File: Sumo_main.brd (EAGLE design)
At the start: 45 x 50 mm, 32 parts, among them U1 ATMEGA8U2AU, U2 SN65HVD3082ED, X1 MINI-USB-SCHIELD-32005-201, X2 RS485, X4 IR Sensor 1, X5 IR Sensor 2, X6 IR Sensor 3, Y1 16MHz

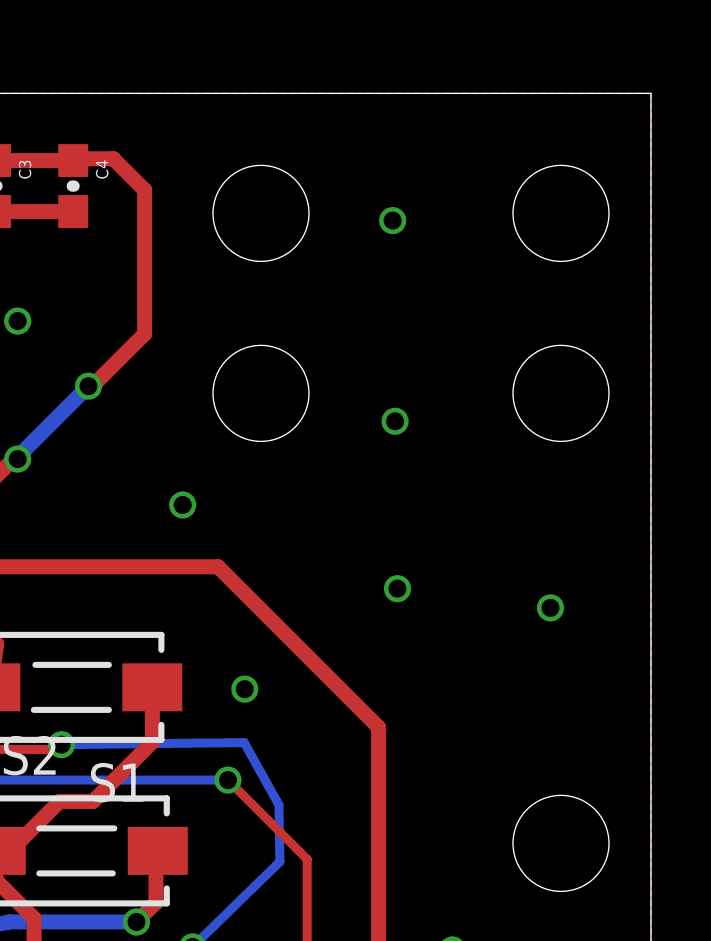
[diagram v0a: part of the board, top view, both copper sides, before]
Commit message: Added PNGs of schematic and board, added text to schematic and board and shortened some components' names.
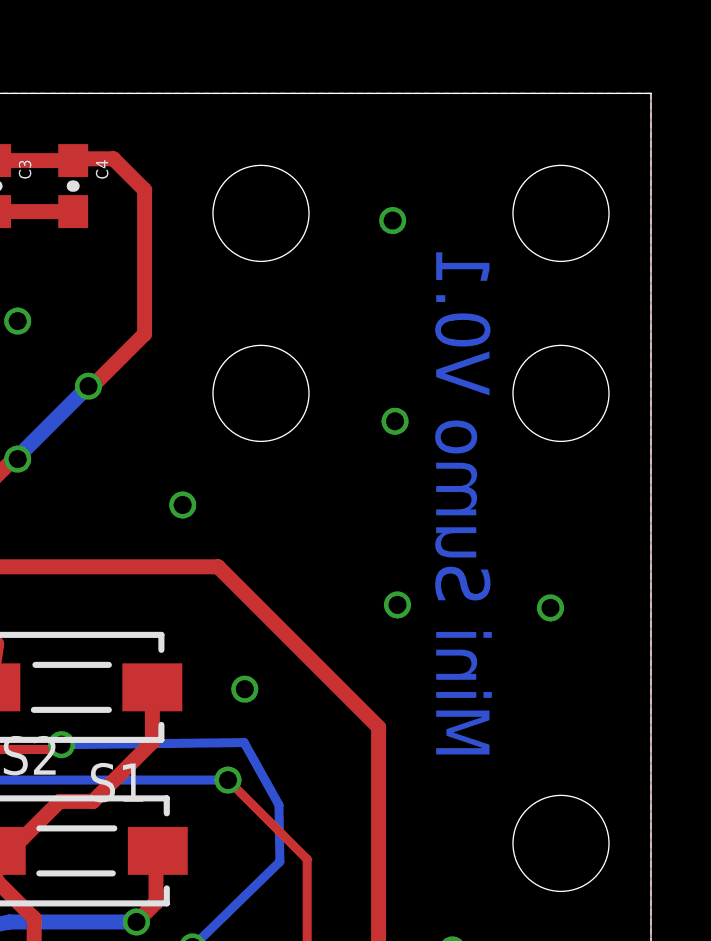
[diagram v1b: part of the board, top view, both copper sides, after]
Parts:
- U2: value SN65HVD3082ED -> SN65HVD3082
- X1: value MINI-USB-SCHIELD-32005-201 -> MINI USB
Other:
- board text added: "Mini Sumo V0.1"
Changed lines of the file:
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@@
 <hole x="32" y="46" drill="3.2"/>
 <hole x="32" y="40" drill="3.2"/>
+<text x="37.84" y="27.75" size="1.778" layer="16" rot="MR90">Mini Sumo V0.1</text>
 </plain>
 <attributes>
@@
 <element name="C3" library="SparkFun-Capacitors" package="0603-CAP" value="100nF" x="23.17" y="46.91" rot="R270"/>
 <element name="C4" library="SparkFun-Capacitors" package="0603-CAP" value="100nF" x="25.74" y="46.91" rot="R270"/>
-<element name="X1" library="con-cypressindustries" package="32005-201" value="MINI-USB-SCHIELD-32005-201" x="5.35" y="43.03">
+<element name="X1" library="con-cypressindustries" package="32005-201" value="MINI USB" x="5.35" y="43.03">
 <attribute name="OC_NEWARK" value="unknown" x="49.8" y="35.41" size="1.778" layer="27" display="off"/>
 <attribute name="MPN" value="" x="49.8" y="35.41" size="1.778" layer="27" display="off"/>
@@
 <attribute name="OC_FARNELL" value="unknown" x="-48.24" y="8.4" size="1.778" layer="27" rot="R270" display="off"/>
 </element>
-<element name="U2" library="SN65HVD3082ED" package="SOIC127P600X175-8N" value="SN65HVD3082ED" x="13.67" y="17.26" rot="R270">
+<element name="U2" library="SN65HVD3082ED" package="SOIC127P600X175-8N" value="SN65HVD3082" x="13.67" y="17.26" rot="R270">
 <attribute name="PACKAGE" value="SOIC-8" x="-10.46" y="-18.3" size="1.778" layer="27" rot="R270" display="off"/>
 <attribute name="OC_NEWARK" value="61H5396" x="-10.46" y="-18.3" size="1.778" layer="27" rot="R270" display="off"/>
@@
 </signal>
 <signal name="N$24">
-<via x="36.55" y="33.49" extent="1-16" drill="0.6"/>
+<via x="36.55" y="32.95" extent="1-16" drill="0.6"/>
 </signal>
 <signal name="N$25">
@@
 </signal>
 </signals>
+<errors>
+</errors>
 </board>
 </drawing>

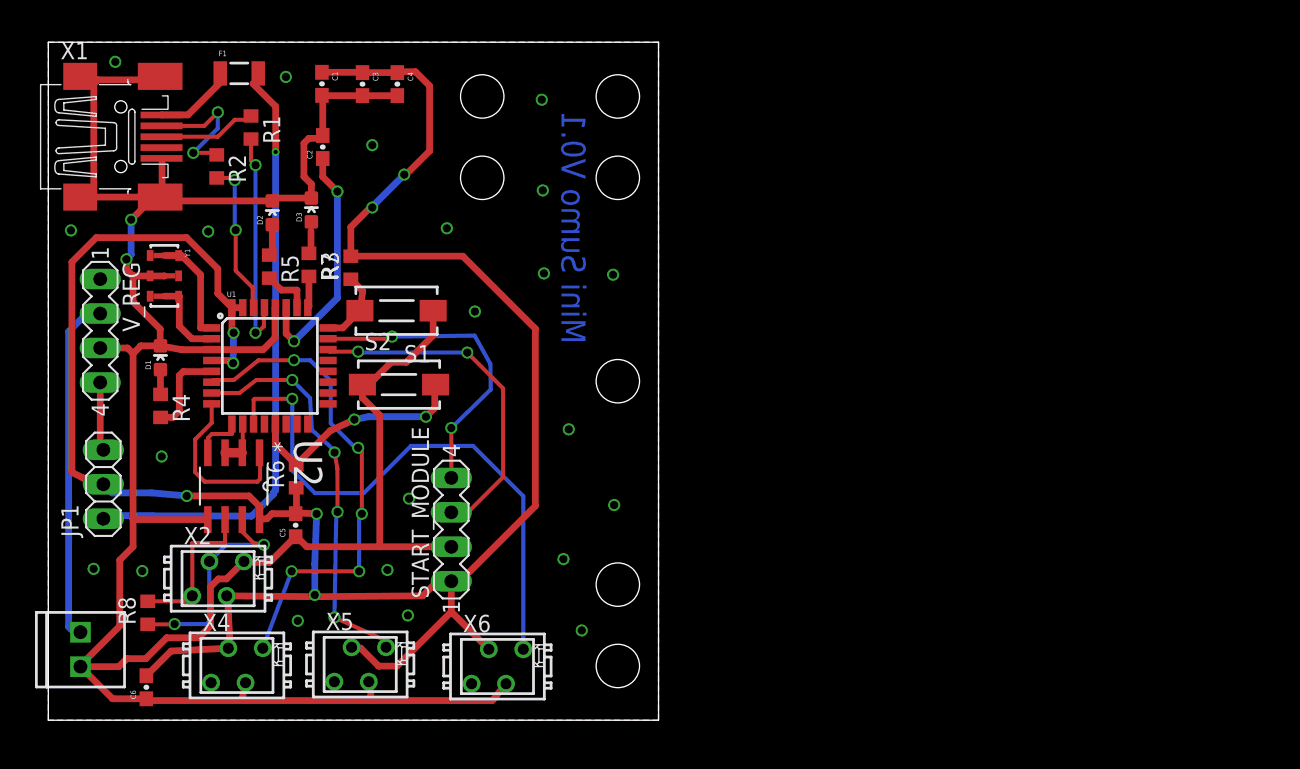
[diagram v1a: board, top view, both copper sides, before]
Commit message: Version 2 - added comparator for sensor signals, redesigned board to be more compact.
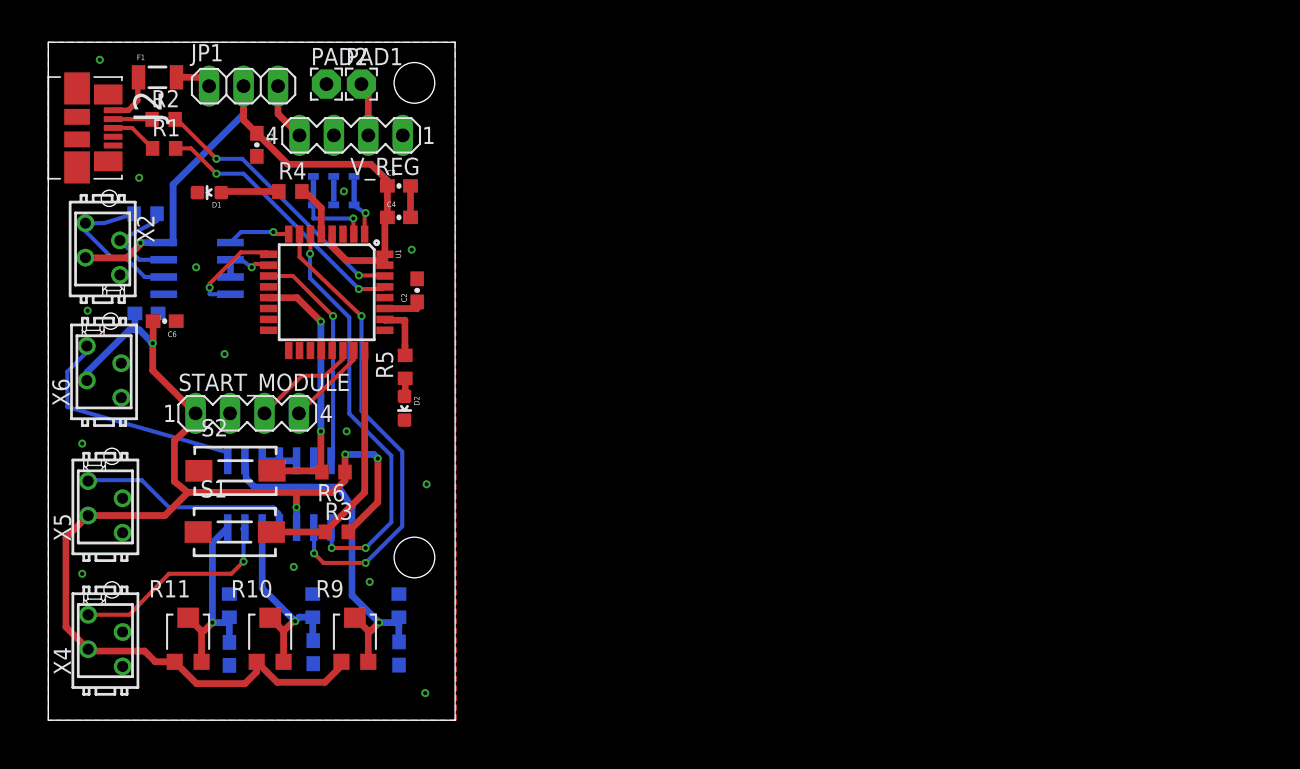
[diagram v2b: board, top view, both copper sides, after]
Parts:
- removed D3: (no value), SparkFun-LED:LED-0603
- removed J1: (no value), SparkFun-Connectors:1X02_2.54_SCREWTERM
- removed R7: 1K, resistor:R0603
- removed X1: MINI USB, con-cypressindustries:32005-201
- added C7, C8, C9: 1uF, SparkFun-Capacitors:0603-CAP
- added J2: (no value), Molex-47346-0001:MOLEX_47346-0001
- added PAD1, PAD2: (no value), wirepad:2,15/1,0
- added R10, R11, R9: 10KOHM, Panasonic-Trimmer_Potentiometers:POT_EVM3W
- added R12, R13, R14: 500R, resistor:R0603
- added U3: LM339D, comparator:SOIC127P600X175-14N
- moved X6 36.2 mm to (4.11, 25.7), turned to 90 degrees
- moved JP1 31.1 mm to (14.4, 46.8), turned to 0 degrees
- moved R8 29.4 mm to (7.17, 37.4), flipped to the bottom, turned to 0 degrees
- moved C6 27.0 mm to (8.58, 29.4), turned to 180 degrees
- moved X2 25.8 mm to (4.01, 34.8), turned to 270 degrees
- moved V_REG 23.4 mm to (22.3, 43.1), turned to 180 degrees
- moved X5 22.1 mm to (4.21, 15.7), turned to 90 degrees
- moved S1 20.2 mm to (13.8, 13.9), turned to 0 degrees
- moved R3 19.5 mm to (21.3, 13.9), turned to 0 degrees
- moved C5 19.1 mm to (7.24, 30.0), flipped to the bottom, turned to 0 degrees
- moved R4 18.5 mm to (17.9, 39.0), turned to 0 degrees
- moved D2 17.4 mm to (26.3, 23.0), turned to 180 degrees
- moved START_MODULE 17.3 mm to (14.7, 22.6), turned to 0 degrees
- moved U2 16.3 mm to (11.0, 33.3), flipped to the bottom, turned to 0 degrees
- moved Y1 14.0 mm to (21.1, 39.0), flipped to the bottom, turned to 0 degrees
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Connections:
- removed net LED3: R7.2, U1.25
- removed net N$8: D3.A, R7.1
- new net COMP_OUT1: U1.6, U3.1
- new net COMP_OUT2: U1.7, U3.2
- new net COMP_OUT3: U1.11, U3.14
- new net VREF1: C7.1, R11.2, R11.3, R14.2, U3.7
- new net VREF2: C9.1, R10.2, R10.3, R13.2, U3.5
- new net VREF3: C8.1, R12.2, R9.2, R9.3, U3.9
- net GND: now also C7.2, C8.2, C9.2, J2.5, PAD2.1, R12.1, R13.1, R14.1, U3.10, U3.11, U3.12; no longer D3.C, J1.P2, X1.5, X1.M1, X1.M2, X1.M3, X1.M4
- net N$1: now also J2.3; no longer X1.3
- net N$2: now also J2.2; no longer X1.2
- net N$23: now also PAD1.1; no longer J1.P1
- net N$3: now also J2.1; no longer X1.1
- net V01: now also U3.6; no longer U1.6
- net V02: now also U3.4; no longer U1.7
- net V03: now also U3.8; no longer U1.11
- net VCC: now also R10.1, R11.1, R9.1, U3.3
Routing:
- net GND: track 204.9 -> 4.86 mm, vias 2 -> 14
- net N$12: track 45.2 -> 2.68 mm, vias 1 -> 0
- net VCC: track 174.5 -> 137.9 mm, vias 7 -> 5
- net COMP_OUT2: track 0.00 -> 34.6 mm, vias 0 -> 3
- net COMP_OUT1: track 0.00 -> 30.5 mm, vias 0 -> 3
- net VREF3: track 0.00 -> 27.6 mm, vias 0 -> 1
- net V03: track 41.9 -> 18.0 mm, vias 1 -> 0
- net N$23: track 26.2 -> 4.00 mm
- net V01: track 36.2 -> 15.7 mm, vias 5 -> 1
- net START: track 25.5 -> 8.06 mm, vias 2 -> 0
- net COMP_OUT3: track 0.00 -> 16.7 mm, vias 0 -> 1
- net KILL: track 22.9 -> 6.34 mm, vias 2 -> 0
- net VREF2: track 0.00 -> 15.9 mm, vias 0 -> 1
- net VREF1: track 0.00 -> 15.5 mm, vias 0 -> 1
- net N$7: track 18.0 -> 2.87 mm, vias 2 -> 0
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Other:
- board size 45 x 50 mm -> 30 x 50 mm
- board text removed: "Mini Sumo V0.1"

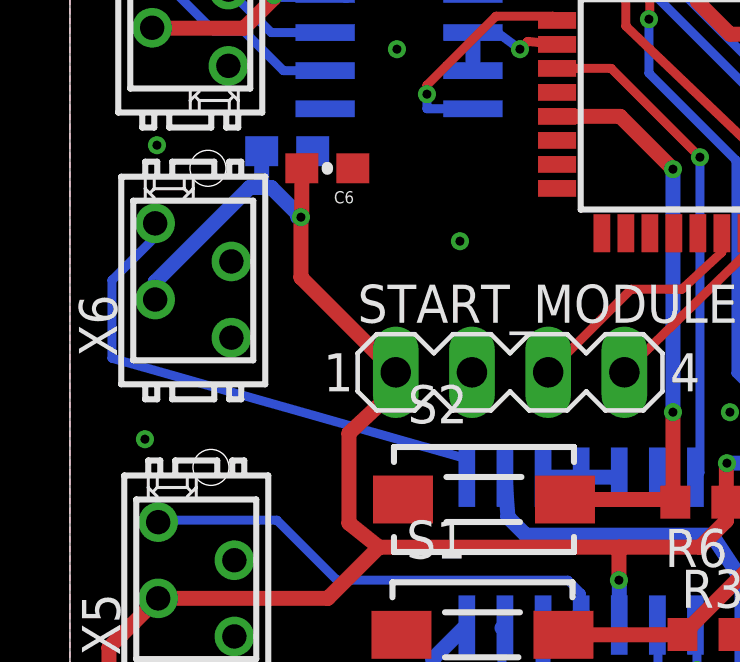
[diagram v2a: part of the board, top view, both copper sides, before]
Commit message: Re-routed X6 signal and VCC.
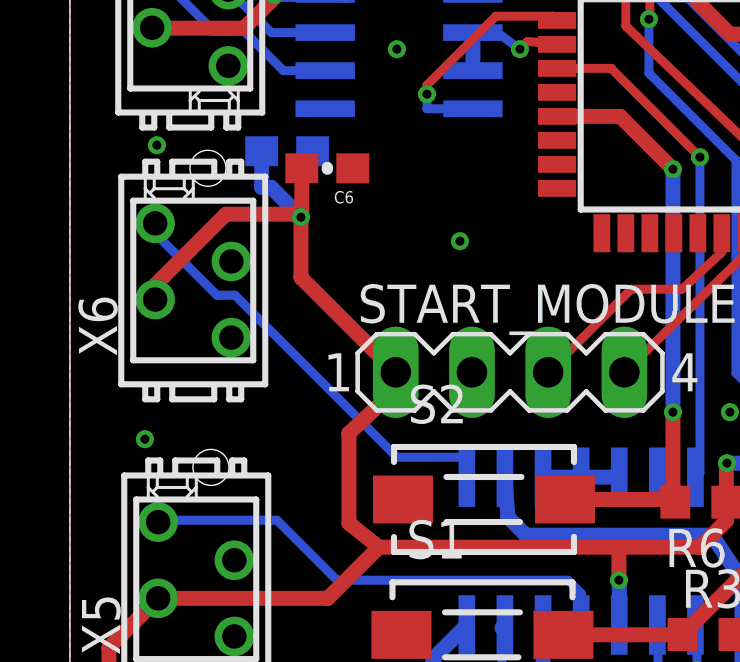
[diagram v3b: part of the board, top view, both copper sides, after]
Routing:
- net V03: track 18.0 -> 14.5 mm
- net VCC: track 137.9 -> 138.8 mm
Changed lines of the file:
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@@
 <wire x1="24.8226" y1="36.8926" x2="24.8226" y2="34.36" width="0.5" layer="1"/>
 <wire x1="24.8226" y1="34.36" x2="24.8226" y2="33.56" width="0.5" layer="1"/>
-<wire x1="5.99" y1="28.79" x2="2.84" y2="25.64" width="0.5" layer="16"/>
-<wire x1="2.84" y1="25.64" x2="2.84" y2="25.055" width="0.5" layer="16"/>
 <wire x1="7.59" y1="27.8" x2="7.7" y2="27.8" width="0.5" layer="16"/>
 <via x="7.7" y="27.8" extent="1-16" drill="0.3"/>
@@
 <wire x1="21.9" y1="19.6" x2="21.88" y2="19.58" width="0.5" layer="1"/>
 <wire x1="21.88" y1="19.58" x2="21.88" y2="18.3" width="0.5" layer="1"/>
-<wire x1="5.99" y1="28.79" x2="6.4" y2="28.79" width="0.5" layer="16"/>
 <wire x1="6.4" y1="28.79" x2="6.71" y2="28.79" width="0.5" layer="16"/>
 <wire x1="6.71" y1="28.79" x2="7.7" y2="27.8" width="0.5" layer="16"/>
@@
 <wire x1="9.3" y1="20.6" x2="10.86" y2="22.06" width="0.5" layer="1"/>
 <wire x1="10.86" y1="22.06" x2="10.86" y2="22.63" width="0.5" layer="1"/>
+<wire x1="2.84" y1="25.055" x2="2.84" y2="25.54" width="0.5" layer="1"/>
+<wire x1="2.84" y1="25.54" x2="5.2" y2="27.9" width="0.5" layer="1"/>
+<wire x1="5.2" y1="27.9" x2="7.6" y2="27.9" width="0.5" layer="1"/>
+<wire x1="7.6" y1="27.9" x2="7.7" y2="27.8" width="0.5" layer="1"/>
 <wire x1="6.39" y1="30" x2="5.8" y2="34.1" width="0" layer="19" extent="1-16"/>
 </signal>
@@
 <contactref element="X6" pad="1"/>
 <contactref element="U3" pad="8"/>
-<wire x1="2.84" y1="27.595" x2="2.84" y2="27.14" width="0.3" layer="16"/>
-<wire x1="2.84" y1="27.14" x2="1.4" y2="25.7" width="0.3" layer="16"/>
-<wire x1="1.4" y1="25.7" x2="1.4" y2="23.1" width="0.3" layer="16"/>
-<wire x1="1.4" y1="23.1" x2="13.2662" y2="19.7338" width="0.3" layer="16"/>
-<wire x1="13.2662" y1="19.7338" x2="13.23" y2="19.1338" width="0.3" layer="16"/>
+<wire x1="2.84" y1="27.595" x2="2.84" y2="27.26" width="0.3" layer="16"/>
+<wire x1="2.84" y1="27.26" x2="4.9" y2="25.2" width="0.3" layer="16"/>
+<wire x1="4.9" y1="25.2" x2="5.5" y2="25.2" width="0.3" layer="16"/>
+<wire x1="5.5" y1="25.2" x2="10.9" y2="19.8" width="0.3" layer="16"/>
+<wire x1="10.9" y1="19.8" x2="13.23" y2="19.8" width="0.3" layer="16"/>
+<wire x1="13.23" y1="19.8" x2="13.23" y2="19.1338" width="0.3" layer="16"/>
 </signal>
 <signal name="RX">

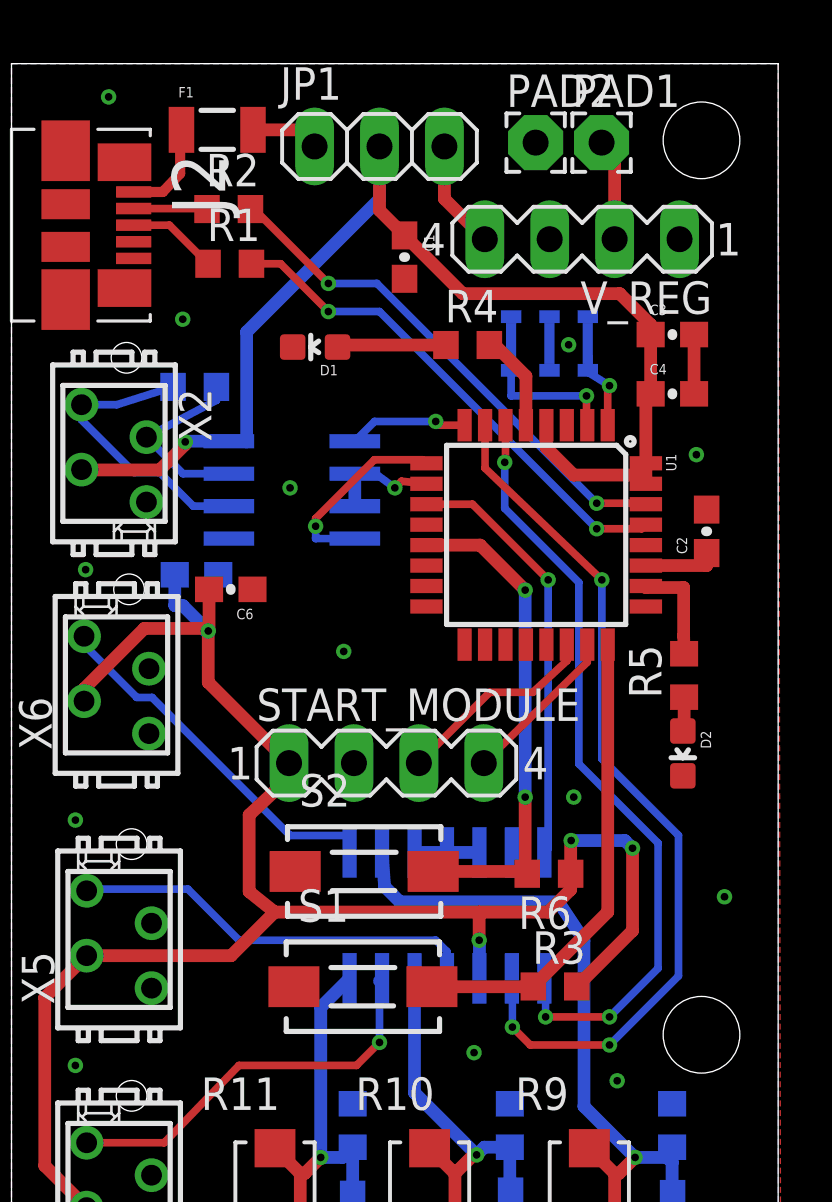
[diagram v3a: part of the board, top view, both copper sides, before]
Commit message: Moved ATMEGA more to center of the board.
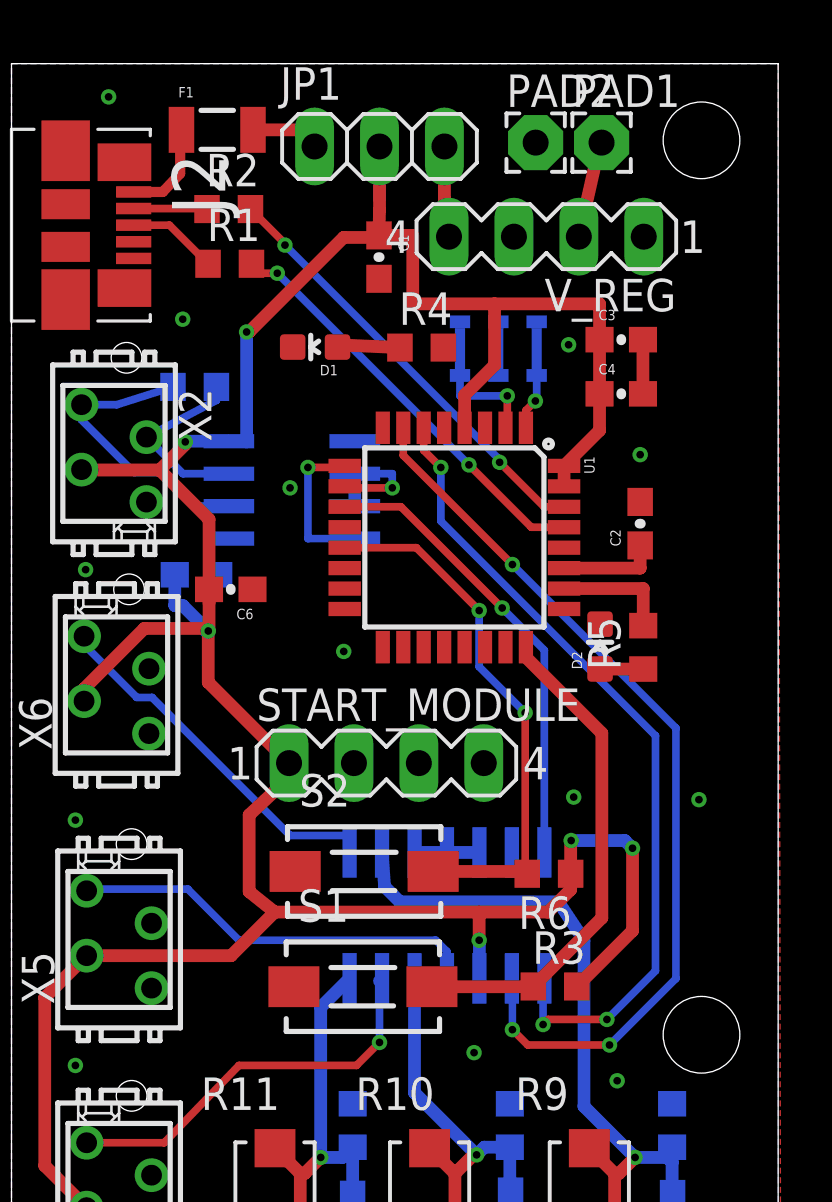
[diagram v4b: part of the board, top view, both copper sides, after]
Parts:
- moved D2 5.29 mm to (23.0, 27.2), turned to 0 degrees
- moved U1 3.20 mm to (17.3, 31.5)
- moved C2 2.62 mm to (24.6, 32.0)
- moved C3 2.01 mm to (23.9, 39.2)
- moved Y1 2.01 mm to (19.1, 38.9)
- moved C4 2.00 mm to (23.9, 37.1)
- moved R5 1.94 mm to (24.7, 27.2)
- moved R4 1.80 mm to (16.1, 38.9)
- moved V_REG 1.40 mm to (20.9, 43.2)
- moved C1 1.00 mm to (14.4, 42.4)
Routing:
- net START: track 8.06 -> 0.00 mm
- net KILL: track 6.34 -> 0.00 mm
- net VCC: track 138.8 -> 144.8 mm, vias 5 -> 6
- net RX: track 4.68 -> 0.00 mm, vias 1 -> 0
- net LED1: track 3.95 -> 0.00 mm
- net D+: track 19.8 -> 16.5 mm
- net D-: track 20.3 -> 17.2 mm
- net N$10: track 4.28 -> 2.49 mm
- net COMP_OUT1: track 30.5 -> 32.1 mm
- net N$13: track 19.4 -> 21.1 mm
- net TX: track 7.67 -> 6.12 mm
- net COMP_OUT3: track 16.7 -> 18.1 mm
- net N$6: track 6.30 -> 5.02 mm
- net COMP_OUT2: track 34.6 -> 35.7 mm
- net N$4: track 18.6 -> 19.6 mm
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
